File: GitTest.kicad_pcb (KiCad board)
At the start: 2 copper layers, 61.7 x 41.1 mm, 3 parts

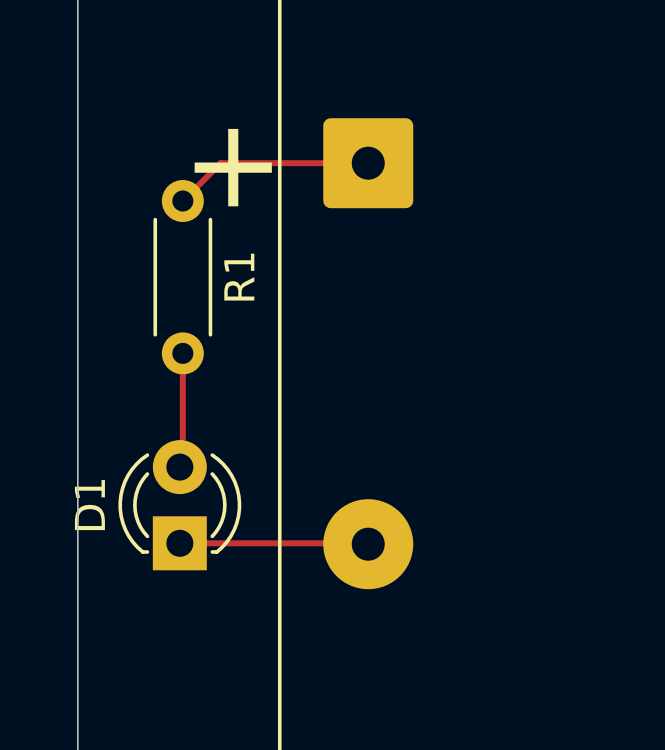
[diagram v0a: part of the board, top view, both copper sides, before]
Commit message: Route new SMD
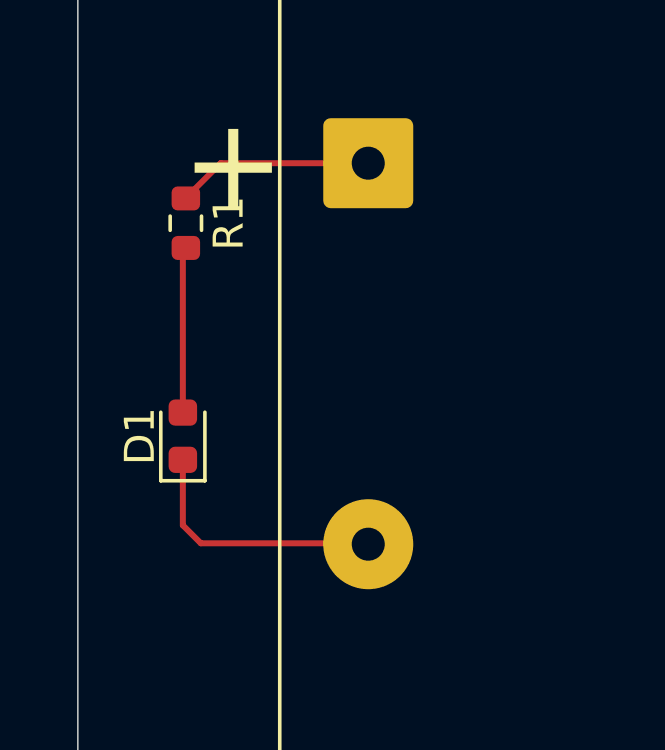
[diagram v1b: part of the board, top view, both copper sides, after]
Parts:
- D1: footprint LED_THT:LED_D3.0mm -> LED_SMD:LED_0603_1608Metric
- R1: footprint Resistor_THT:R_Axial_DIN0204_L3.6mm_D1.6mm_P5.08mm_Horizontal -> Resistor_SMD:R_0603_1608Metric
- moved D1 3.57 mm to (116.5, 105.1)
- moved R1 0.75 mm to (116.6, 98.0)
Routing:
- net GND: track 6.29 -> 8.62 mm
- net Net-(D1-A): track 3.83 -> 5.17 mm
